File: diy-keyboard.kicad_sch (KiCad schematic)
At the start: 16 parts

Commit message: Update Library and schematic
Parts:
- added F?: 500mA, symbol Device:Polyfuse_Small
- added R? (x2): 5.1K, symbol Device:R_Small
- added U?: PRTR5V0U2X, Package_TO_SOT_SMD:SOT-143, symbol PWR_protection:PRTR5V0U2X
- added USB?: HRO-TYPE-C-31-M-12, symbol Type-C:HRO-TYPE-C-31-M-12
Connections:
- net +5V: now also F?.2
- net GND: now also R?.2, R?.2, U?.1 (GND), USB?.1 (GND), USB?.12 (GND), USB?.13 (SHIELD)
- net at R?.2: now also U?.3 (D-); no longer U?.4 (D+)
- net at R?.2: now also U?.4 (D+); no longer U?.3 (D-)
- net D+: no longer names the net of R?.1
- net D+: now also U?.3 (IO2), USB?.5 (DN2), USB?.7 (DN1)
- net D-: no longer names the net of R?.1
- net D-: now also U?.2 (IO1), USB?.6 (DP1), USB?.8 (DP2)
- net MISO: no longer names the net of J?.1 (MISO), U?.11 (PB3)
- net MOSI: no longer names the net of J?.4 (MOSI), U?.10 (PB2)
- net SCK: no longer names the net of J?.3 (SCK), U?.9 (PB1)
- new net: R?.1, USB?.10 (CC2)
- new net: R?.1, USB?.4 (CC1)
- new net VCC: F?.1, U?.4 (VCC), USB?.11 (VBUS), USB?.2 (VBUS)
- no-connect marks 3 -> 5
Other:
- added sheet Matrix_SW (Matrix_SW.kicad_sch)
- moved on the sheet: C?, J?, R?, SW?, U?, Y?

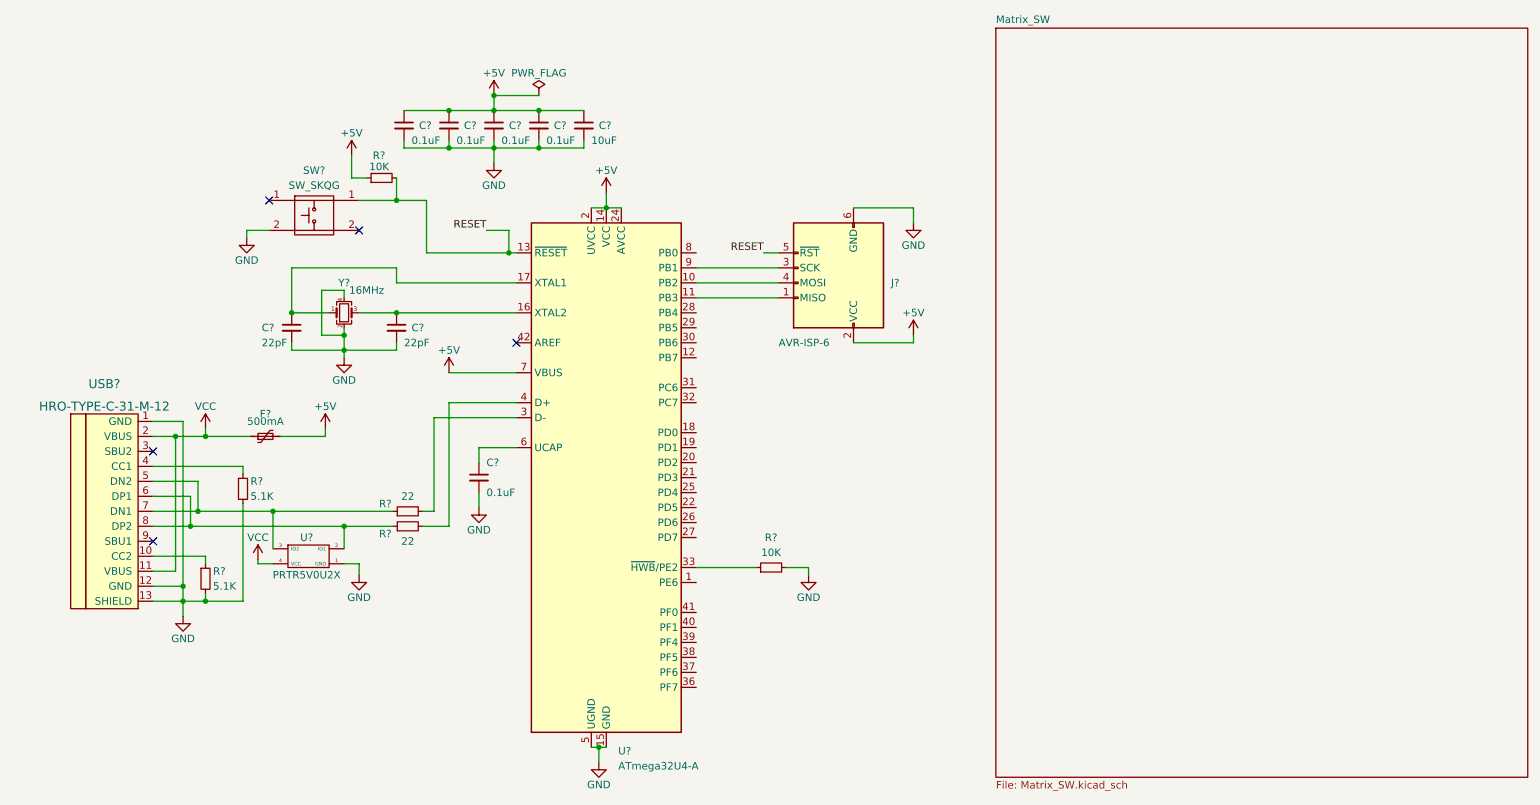
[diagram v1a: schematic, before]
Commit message: Update schematic connecting matrix keyboard switch to MCU
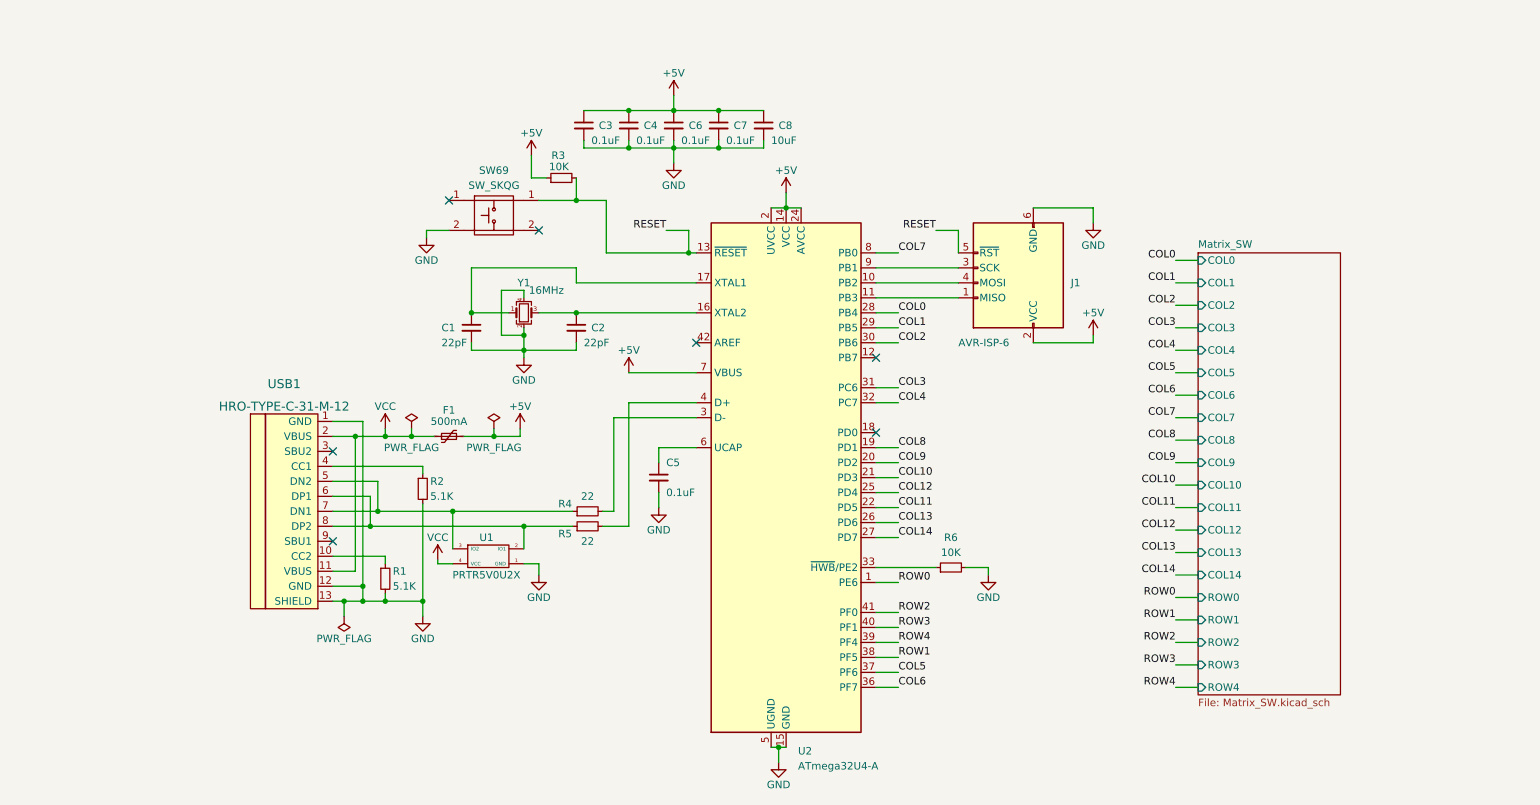
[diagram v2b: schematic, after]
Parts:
- gave numbers to parts that had none: 21
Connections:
- net ROW0: now reaches U2.1 (PE6)
- net COL8: now reaches U2.19 (PD1)
- net COL9: now reaches U2.20 (PD2)
- net COL10: now reaches U2.21 (PD3)
- net COL11: now reaches U2.22 (PD5)
- net COL12: now reaches U2.25 (PD4)
- net COL13: now reaches U2.26 (PD6)
- net COL14: now reaches U2.27 (PD7)
- net COL0: now reaches U2.28 (PB4)
- net COL1: now reaches U2.29 (PB5)
- net COL2: now reaches U2.30 (PB6)
- net COL3: now reaches U2.31 (PC6)
- net COL4: now reaches U2.32 (PC7)
- net COL6: now reaches U2.36 (PF7)
- net COL5: now reaches U2.37 (PF6)
- net ROW1: now reaches U2.38 (PF5)
- net ROW4: now reaches U2.39 (PF4)
- net ROW3: now reaches U2.40 (PF1)
- net ROW2: now reaches U2.41 (PF0)
- net COL7: now reaches U2.8 (PB0)
- no-connect marks 5 -> 7
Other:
- sheet Matrix_SW ports: added COL0, COL1, COL10, COL11, COL12, COL13, COL14, COL2, COL3, COL4, COL5, COL6, COL7, COL8, COL9, ROW0, ROW1, ROW2, ROW3, ROW4; removed none
- moved on the sheet: C1, C2, C3, C4, C5, C6, C7, C8, F1, J1, R1, R2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

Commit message: Assigning footprint to components
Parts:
- C1, C2, C3, C4, C5, C6, C7, C8: footprint (none) -> Capacitor_SMD:C_0805_2012Metric_Pad1.18x1.45mm_HandSolder
- F1: footprint (none) -> Fuse:Fuse_1206_3216Metric_Pad1.42x1.75mm_HandSolder
- J1: footprint (none) -> ISP-header:Reset_Pretty-Mask
- R1, R2, R3, R4, R5, R6: footprint (none) -> Resistor_SMD:R_0805_2012Metric_Pad1.20x1.40mm_HandSolder
- SW69: footprint (none) -> Button_Switch_SMD:SW_SPST_SKQG_WithoutStem
- U1: footprint Package_TO_SOT_SMD:SOT-143 -> Package_TO_SOT_SMD:SOT-143_Handsoldering
- USB1: footprint (none) -> Type-C:HRO-TYPE-C-31-M-12-HandSoldering
- Y1: footprint (none) -> Crystal:Crystal_SMD_3225-4Pin_3.2x2.5mm_HandSoldering

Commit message: Making edge cuts PCB taking a shape
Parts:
- SW69: footprint Button_Switch_SMD:SW_SPST_SKQG_WithoutStem -> Button_Switch_SMD:SW_SPST_SKQG_WithStem
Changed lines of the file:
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@@
     (property "Reference" "SW69" (id 0) (at 99.06 49.53 0))
     (property "Value" "SW_SKQG" (id 1) (at 99.06 52.07 0))
-    (property "Footprint" "Button_Switch_SMD:SW_SPST_SKQG_WithoutStem" (id 2) (at 99.06 49.53 0)
+    (property "Footprint" "Button_Switch_SMD:SW_SPST_SKQG_WithStem" (id 2) (at 99.06 49.53 0)
       (effects (font (size 1.27 1.27)) hide)
     )
@@
     )
     (path "/465b5513-5b40-42d0-872d-c9f3d12b47ef"
-      (reference "SW69") (unit 1) (value "SW_SKQG") (footprint "Button_Switch_SMD:SW_SPST_SKQG_WithoutStem")
+      (reference "SW69") (unit 1) (value "SW_SKQG") (footprint "Button_Switch_SMD:SW_SPST_SKQG_WithStem")
     )
     (path "/537a57f8-16a0-40fe-84df-a4ed4c941e42"

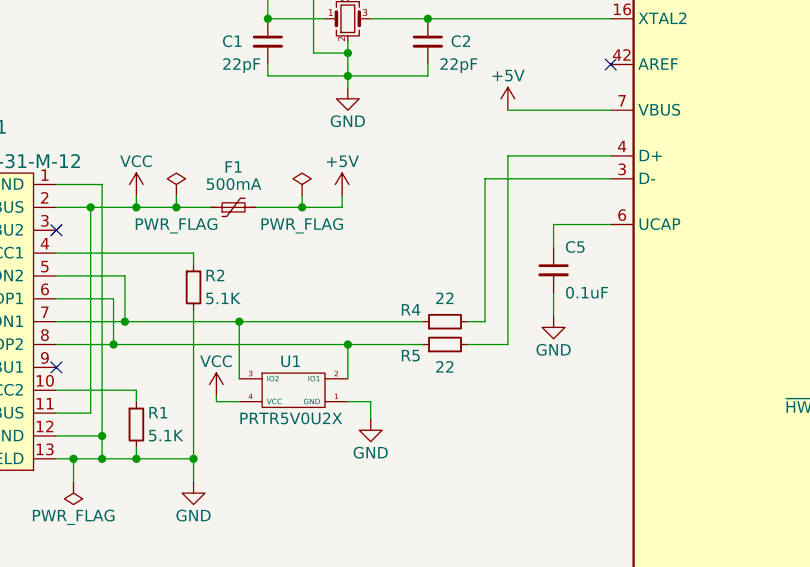
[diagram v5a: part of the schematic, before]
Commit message: Add label for diferential pair
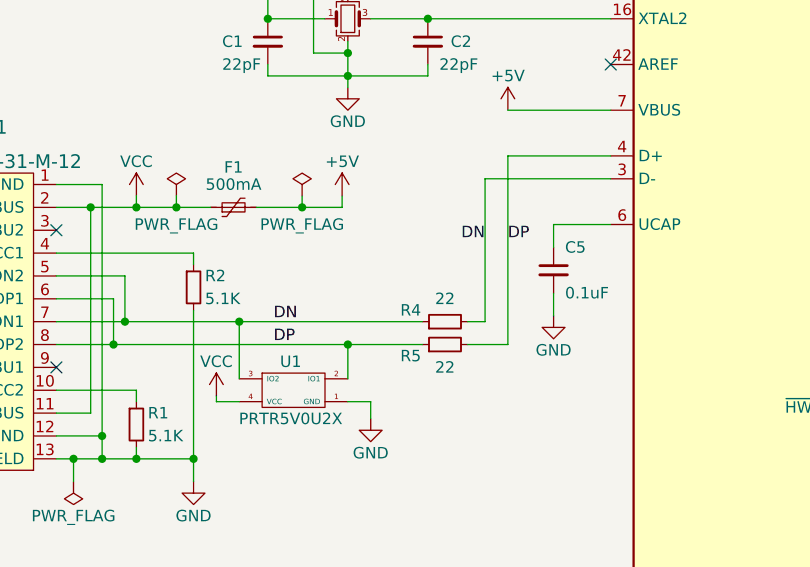
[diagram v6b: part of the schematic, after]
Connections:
- net DN: now reaches R4.1, U1.3 (IO2), USB1.5 (DN2), USB1.7 (DN1)
- net DN: now also R4.2, U2.3 (D-)
- net DP: now reaches R5.1, U1.2 (IO1), USB1.6 (DP1), USB1.8 (DP2)
- net DP: now also R5.2, U2.4 (D+)
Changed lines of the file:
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@@
+    (effects (font (size 1.27 1.27)) (justify left bottom))
+  )
+  (label "DP" (at 95.885 109.855 0)
     (effects (font (size 1.27 1.27)) (justify left bottom))
   )
@@
     (effects (font (size 1.27 1.27)) (justify right bottom))
   )
+  (label "DN" (at 119.38 98.425 180)
+    (effects (font (size 1.27 1.27)) (justify right bottom))
+  )
   (label "COL0" (at 167.64 73.66 0)
     (effects (font (size 1.27 1.27)) (justify left bottom))
@@
     (effects (font (size 1.27 1.27)) (justify left bottom))
   )
+  (label "DP" (at 121.92 98.425 0)
+    (effects (font (size 1.27 1.27)) (justify left bottom))
+  )
   (label "COL14" (at 214.63 118.11 180)
     (effects (font (size 1.27 1.27)) (justify right bottom))
@@
     (effects (font (size 1.27 1.27)) (justify left bottom))
   )
+  (label "DN" (at 95.885 107.315 0)
+    (effects (font (size 1.27 1.27)) (justify left bottom))
+  )

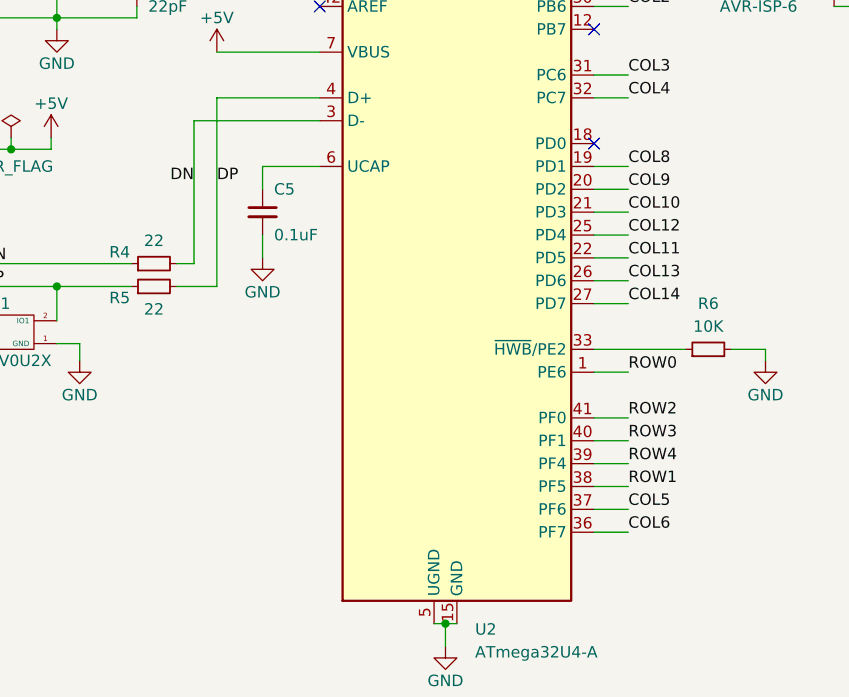
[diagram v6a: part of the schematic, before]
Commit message: Reassign footprint SW59 and re-allign keyboard layout
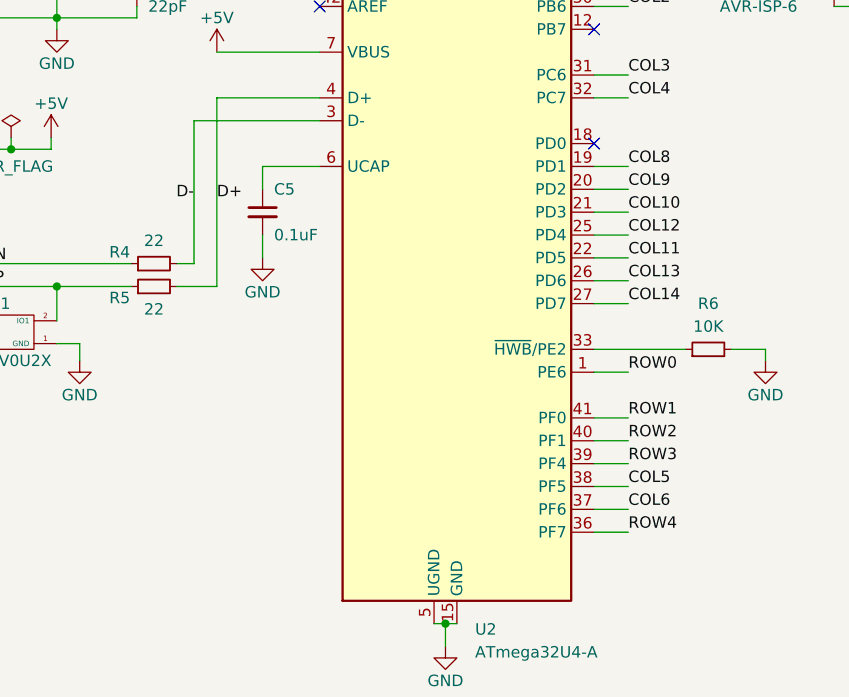
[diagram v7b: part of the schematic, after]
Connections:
- net COL5: now also U2.38 (PF5); no longer U2.37 (PF6)
- net COL6: now also U2.37 (PF6); no longer U2.36 (PF7)
- net DN: no longer R4.2, U2.3 (D-)
- net DP: no longer R5.2, U2.4 (D+)
- net ROW1: now also U2.41 (PF0); no longer U2.38 (PF5)
- net ROW2: now also U2.40 (PF1); no longer U2.41 (PF0)
- net ROW3: now also U2.39 (PF4); no longer U2.40 (PF1)
- net ROW4: now also U2.36 (PF7); no longer U2.39 (PF4)
- new net D+: R5.2, U2.4 (D+)
- new net D-: R4.2, U2.3 (D-)
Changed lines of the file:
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@@
     (effects (font (size 1.27 1.27)) (justify right bottom))
   )
-  (label "ROW3" (at 167.64 127 0)
+  (label "ROW3" (at 167.64 129.54 0)
     (effects (font (size 1.27 1.27)) (justify left bottom))
   )
@@
     (effects (font (size 1.27 1.27)) (justify right bottom))
   )
-  (label "DN" (at 119.38 98.425 180)
-    (effects (font (size 1.27 1.27)) (justify right bottom))
-  )
   (label "COL0" (at 167.64 73.66 0)
     (effects (font (size 1.27 1.27)) (justify left bottom))
@@
     (effects (font (size 1.27 1.27)) (justify left bottom))
   )
-  (label "ROW4" (at 167.64 129.54 0)
+  (label "ROW1" (at 167.64 124.46 0)
     (effects (font (size 1.27 1.27)) (justify left bottom))
   )
@@
     (effects (font (size 1.27 1.27)) (justify right bottom))
   )
+  (label "D-" (at 119.38 100.33 180)
+    (effects (font (size 1.27 1.27)) (justify right bottom))
+  )
   (label "COL3" (at 214.63 76.2 180)
     (effects (font (size 1.27 1.27)) (justify right bottom))
   )
+  (label "D+" (at 121.92 100.33 0)
+    (effects (font (size 1.27 1.27)) (justify left bottom))
+  )
   (label "COL0" (at 214.63 64.77 180)
     (effects (font (size 1.27 1.27)) (justify right bottom))
@@
     (effects (font (size 1.27 1.27)) (justify left bottom))
   )
-  (label "DP" (at 121.92 98.425 0)
-    (effects (font (size 1.27 1.27)) (justify left bottom))
-  )
   (label "COL14" (at 214.63 118.11 180)
     (effects (font (size 1.27 1.27)) (justify right bottom))
@@
     (effects (font (size 1.27 1.27)) (justify right bottom))
   )
-  (label "COL6" (at 167.64 137.16 0)
+  (label "COL6" (at 167.64 134.62 0)
     (effects (font (size 1.27 1.27)) (justify left bottom))
   )
@@
     (effects (font (size 1.27 1.27)) (justify left bottom))
   )
-  (label "ROW1" (at 167.64 132.08 0)
+  (label "ROW4" (at 167.64 137.16 0)
     (effects (font (size 1.27 1.27)) (justify left bottom))
   )
@@
     (effects (font (size 1.27 1.27)) (justify left bottom))
   )
-  (label "COL5" (at 167.64 134.62 0)
-    (effects (font (size 1.27 1.27)) (justify left bottom))
-  )
-  (label "ROW2" (at 167.64 124.46 0)
+  (label "COL5" (at 167.64 132.08 0)
+    (effects (font (size 1.27 1.27)) (justify left bottom))
+  )
+  (label "ROW2" (at 167.64 127 0)
     (effects (font (size 1.27 1.27)) (justify left bottom))
   )
@@
     )
     (path "/d777be28-81e9-43bf-9f82-1a2c0d07f36c/3204c3f7-5790-40f1-bdfa-02200c0bc27c"
-      (reference "SW59") (unit 1) (value "LCTRL") (footprint "Switch_Keyboard_Cherry_MX:SW_Cherry_MX_PCB_1.25u")
+      (reference "SW59") (unit 1) (value "LCTRL") (footprint "Switch_Keyboard_Cherry_MX:SW_Cherry_MX_PCB_1.50u")
     )
     (path "/d777be28-81e9-43bf-9f82-1a2c0d07f36c/13572000-b792-4413-8614-d7fd7a73d6f4"
@@
     )
     (path "/d777be28-81e9-43bf-9f82-1a2c0d07f36c/0eb52074-3687-4095-86dc-760b352ab3d0"
-      (reference "SW63") (unit 1) (value "RALT") (footprint "Switch_Keyboard_Cherry_MX:SW_Cherry_MX_PCB_1.25u")
+      (reference "SW63") (unit 1) (value "RALT") (footprint "Switch_Keyboard_Cherry_MX:SW_Cherry_MX_PCB_1.00u")
     )
     (path "/d777be28-81e9-43bf-9f82-1a2c0d07f36c/64dd963e-9951-4698-a77f-375d928784b8"

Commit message: Change diode footprint to 1N4148 SOD-123 and re-routing PCB
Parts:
- removed SW69: SW_SKQG, Button_Switch_SMD:SW_SPST_SKQG_WithStem, symbol SW_SK:SW_SKQG
- removed U1: PRTR5V0U2X, Package_TO_SOT_SMD:SOT-143_Handsoldering, symbol PWR_protection:PRTR5V0U2X
- removed USB1: HRO-TYPE-C-31-M-12, Type-C:HRO-TYPE-C-31-M-12-HandSoldering, symbol Type-C:HRO-TYPE-C-31-M-12
- added SW69: SW_SKQG, Button_Switch_SMD:SW_SPST_SKQG_WithStem, symbol Local_lib_SW_SK:SW_SKQG
- added U1: PRTR5V0U2X, Package_TO_SOT_SMD:SOT-143, symbol Local_lib_PWR_protection:PRTR5V0U2X
- added USB1: HRO-TYPE-C-31-M-12, Local_lib_Type-C:HRO-TYPE-C-31-M-12-HandSoldering, symbol Local_lib_Type-C:HRO-TYPE-C-31-M-12
- J1: footprint ISP-header:Reset_Pretty-Mask -> Local_lib_ISP-header:Reset_Pretty-Mask
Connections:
- net COL5: now also U2.1 (PE6); no longer U2.38 (PF5)
- net DN: now also U1.3 (IO2), USB1.5 (DN2), USB1.7 (DN1)
- net DP: now also U1.2 (IO1), USB1.6 (DP1), USB1.8 (DP2)
- net GND: now also SW69.2, U1.1 (GND), USB1.1 (GND), USB1.12 (GND), USB1.13 (SHIELD)
- net RESET: now also SW69.1
- net ROW0: now also U2.38 (PF5); no longer U2.1 (PE6)
- net ROW1: now also U2.39 (PF4); no longer U2.41 (PF0)
- net ROW3: now also U2.41 (PF0); no longer U2.39 (PF4)
- net VCC: now also U1.4 (VCC), USB1.11 (VBUS), USB1.2 (VBUS)
- net at R1.1: now also USB1.10 (CC2)
- net at R2.1: now also USB1.4 (CC1)
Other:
- moved on the sheet: F1, R1, R2, R4, R5
